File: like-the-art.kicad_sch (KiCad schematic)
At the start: 4 parts

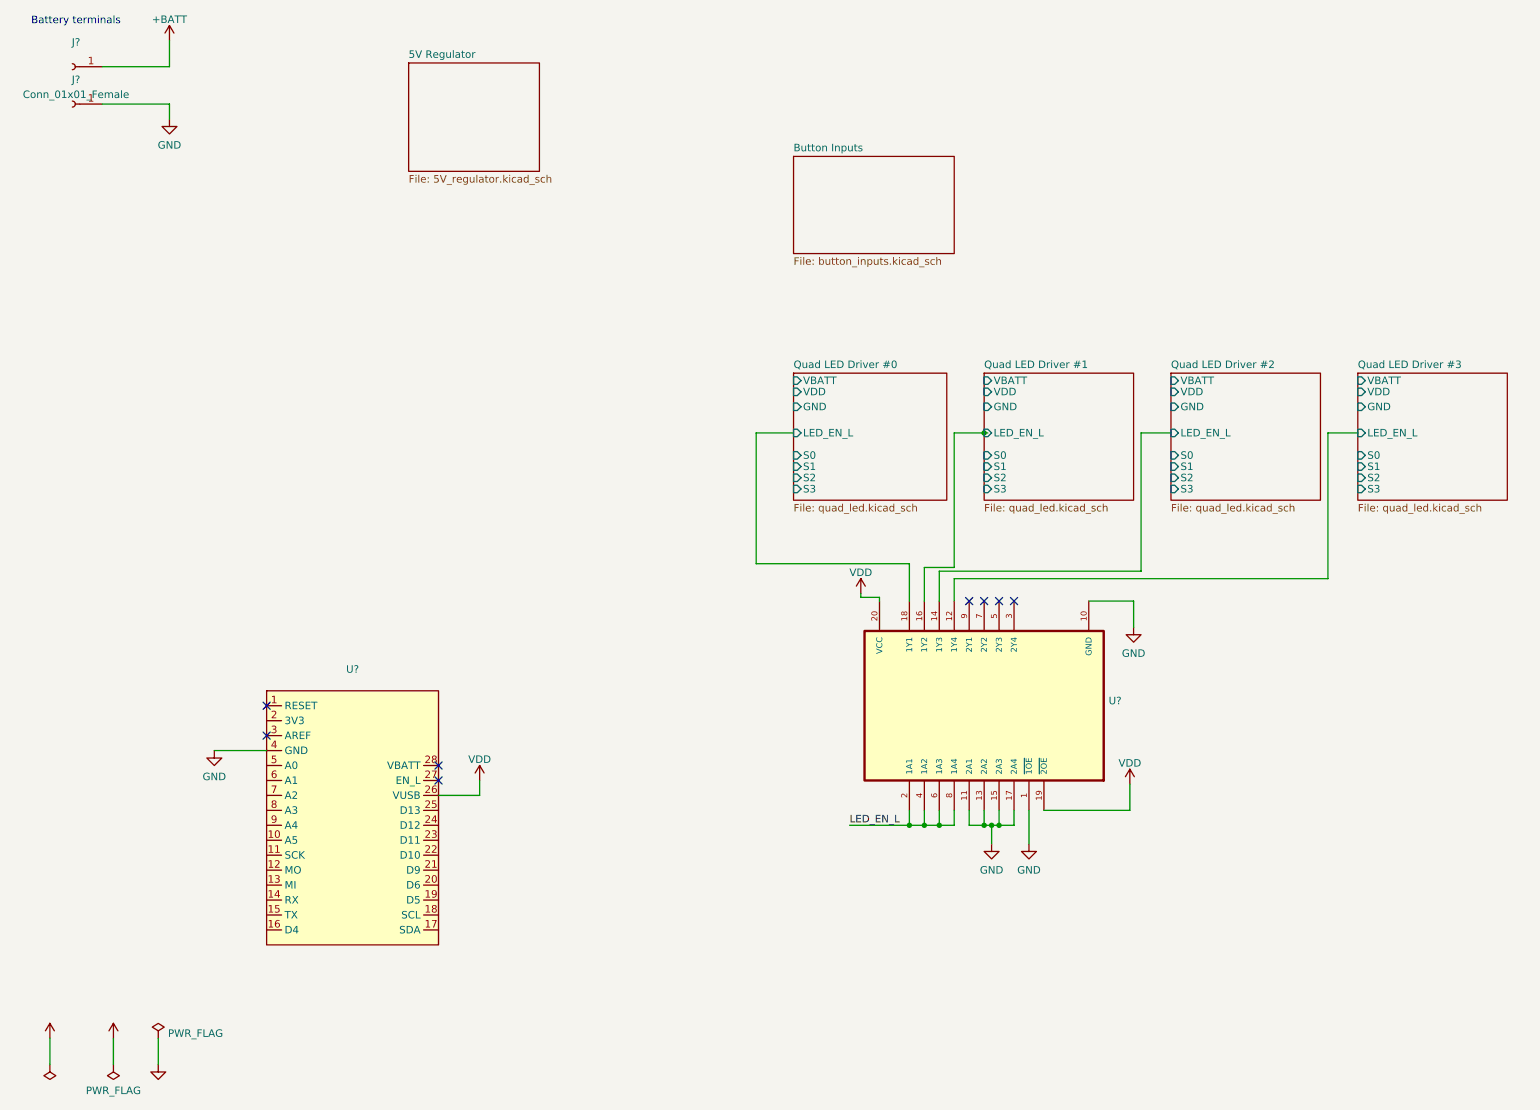
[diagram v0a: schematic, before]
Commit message: Add schematic for button inputs and I2C signal busses.
* Define 9x button inputs
* Define I2C parallel bus expanders used for FET output signals
  and button inputs
* Add (empty) schematic for 5V switching regulator.
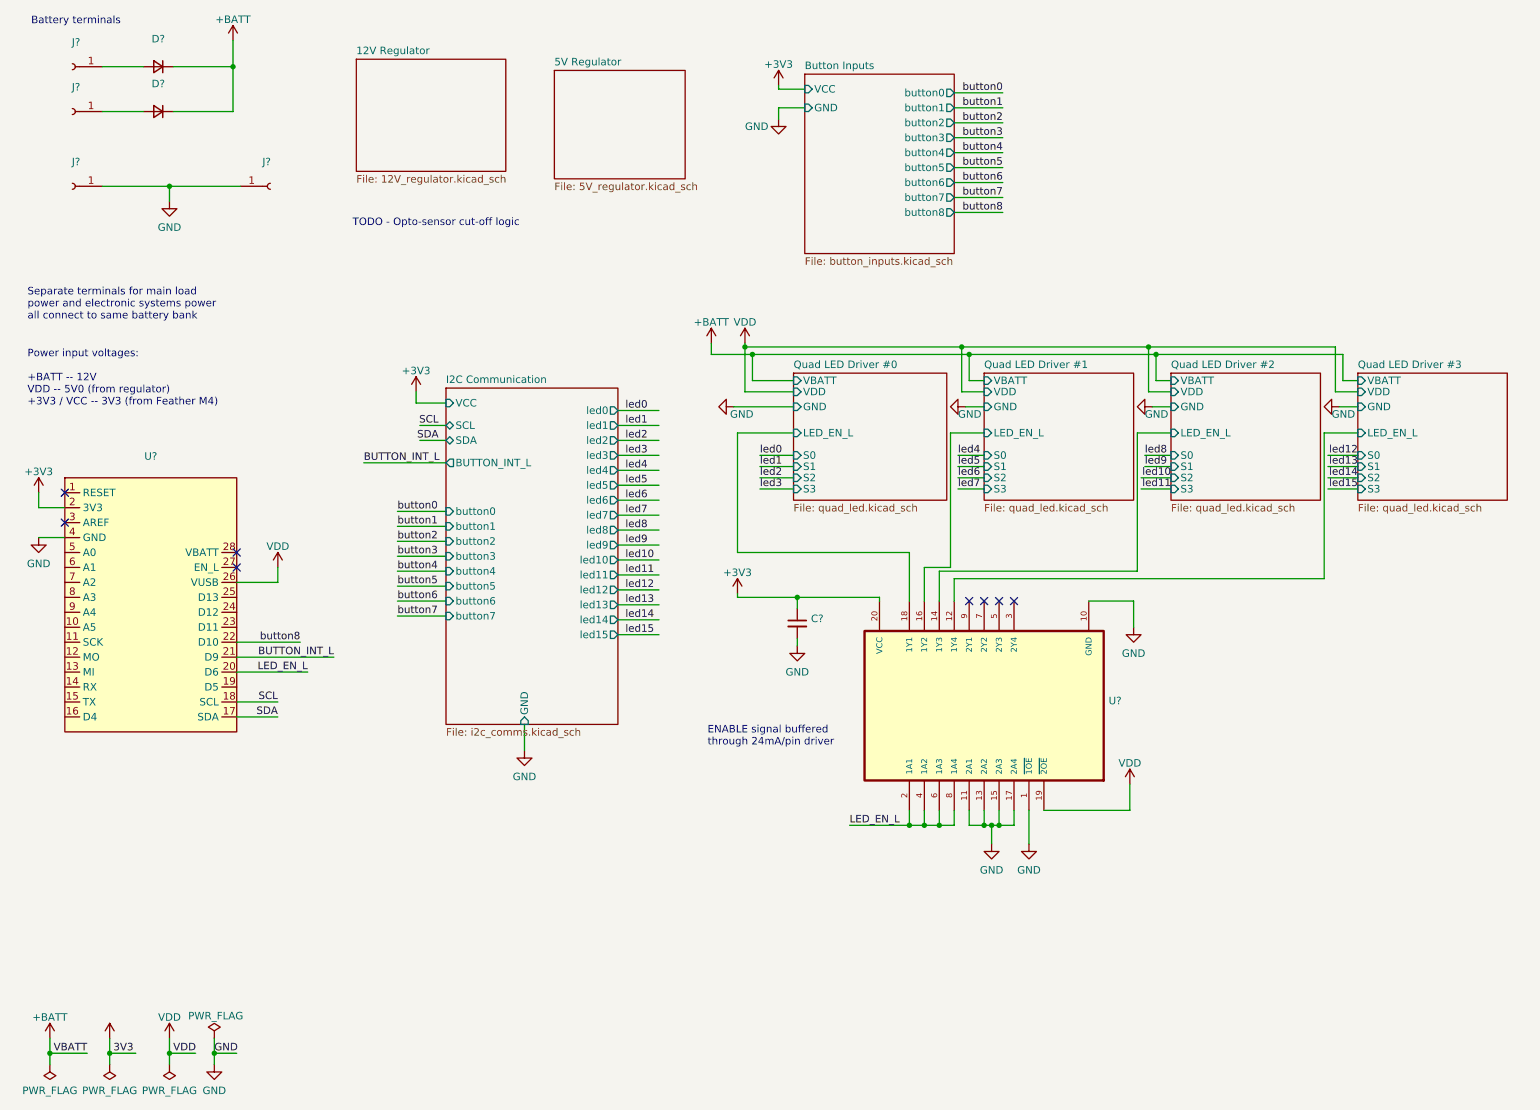
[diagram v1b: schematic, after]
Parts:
- added C?: (no value), symbol Device:C_Small
- added D? (x2): (no value), symbol Device:D_Small
- added J? (x2): (no value), symbol Connector:Conn_01x01_Female
- J?: value Conn_01x01_Female -> (none)
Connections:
- net +BATT: now also D?.1 (K), D?.1 (K); no longer J?.1 (Pin_1)
- net GND: now also C?.2, J?.1 (Pin_1)
- net LED_EN_L: now also U?.20 (D6)
- net VDD: no longer U?.20 (VCC)
- net SDA: now reaches U?.17 (SDA)
- net SCL: now reaches U?.18 (SCL)
- net +3V3: now reaches U?.2 (3V3)
- net +3V3: now also U?.20 (VCC), C?.1
- net BUTTON_INT_L: now reaches U?.21 (D9)
- net button8: now reaches U?.22 (D10)
- new net: D?.2 (A), J?.1 (Pin_1) (x2)
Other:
- added sheet 12V Regulator (12V_regulator.kicad_sch)
- added sheet I2C Communication (i2c_comms.kicad_sch)
- sheet Button Inputs ports: added GND, VCC, button0, button1, button2, button3, button4, button5, button6, button7, button8; removed none
- note added: "ENABLE signal buffered through 24mA/pin driver"
- note added: "Power input voltages: +BATT -- 12V VDD -- 5V0 (from regulator) +3V3 / VCC -- 3V3 (from Feather M4)"
- note added: "Separate terminals for main load power and electronic systems power all connect to same battery bank"
- note added: "TODO - Opto-sensor cut-off logic"
- moved on the sheet: J?, U?

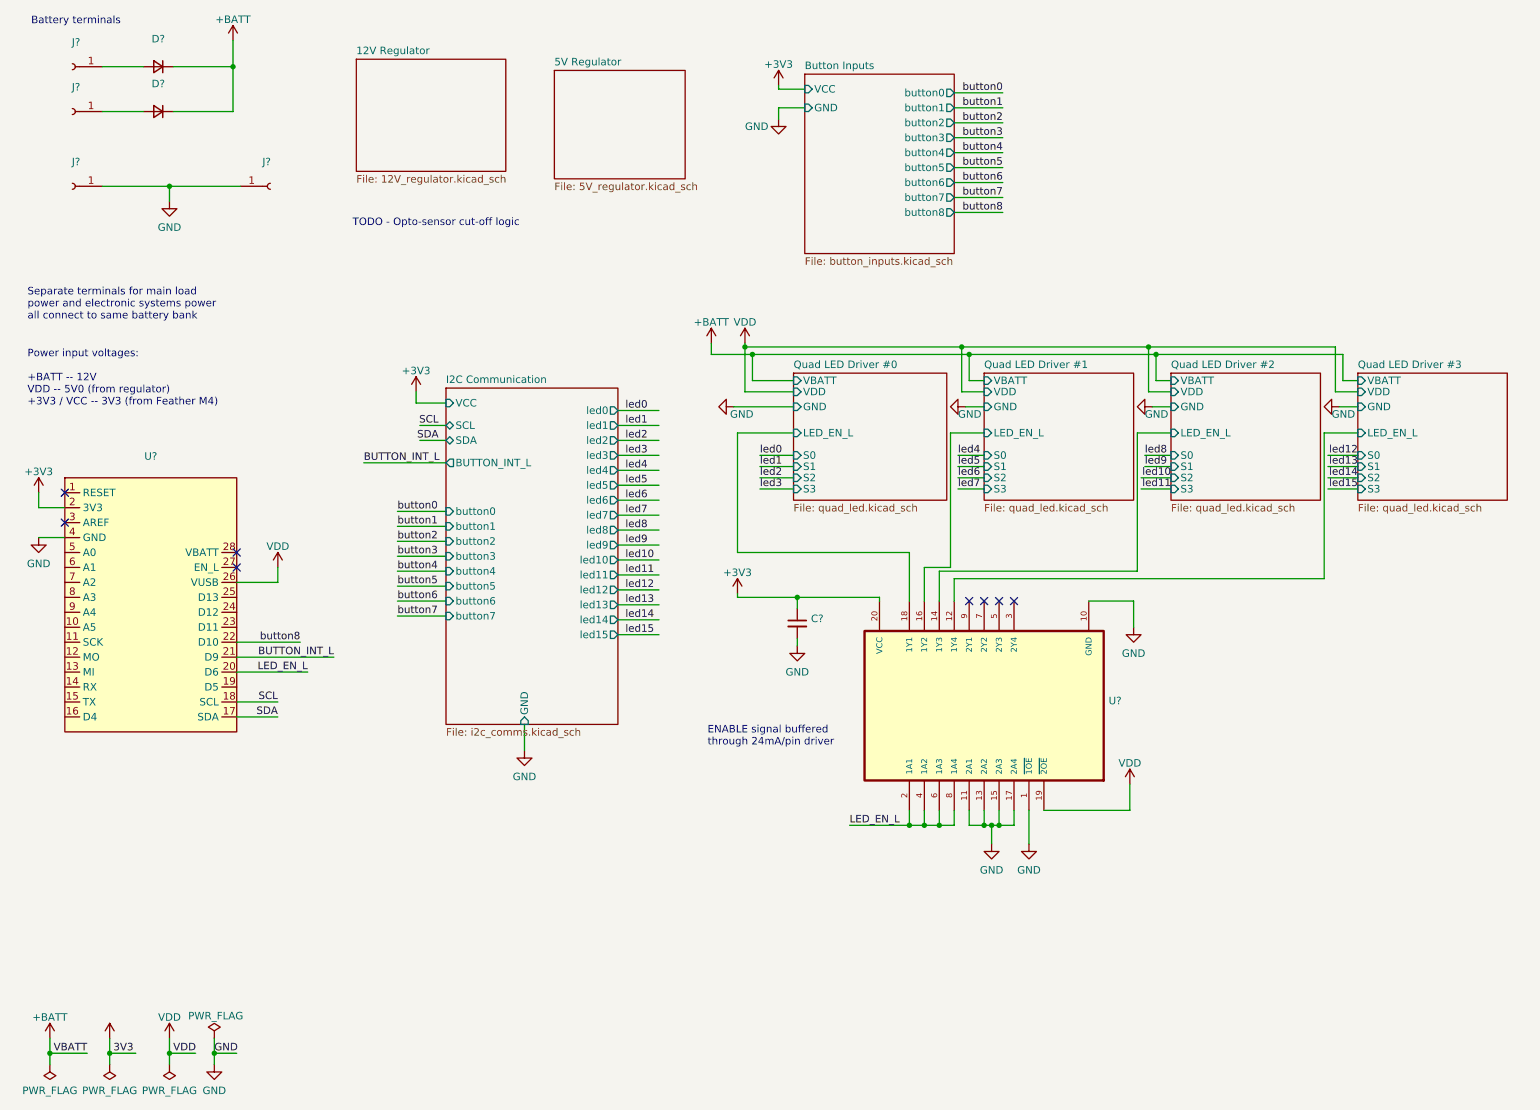
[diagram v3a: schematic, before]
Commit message: Sketch out ISL8117-driven 12V regulator.
Another candidate entry for on-board 12V regulation is to
build our own based on the reference schematic from the ISL8117
DC buck regulator controller datasheet.

Implemented (most of) this reference schematic here.
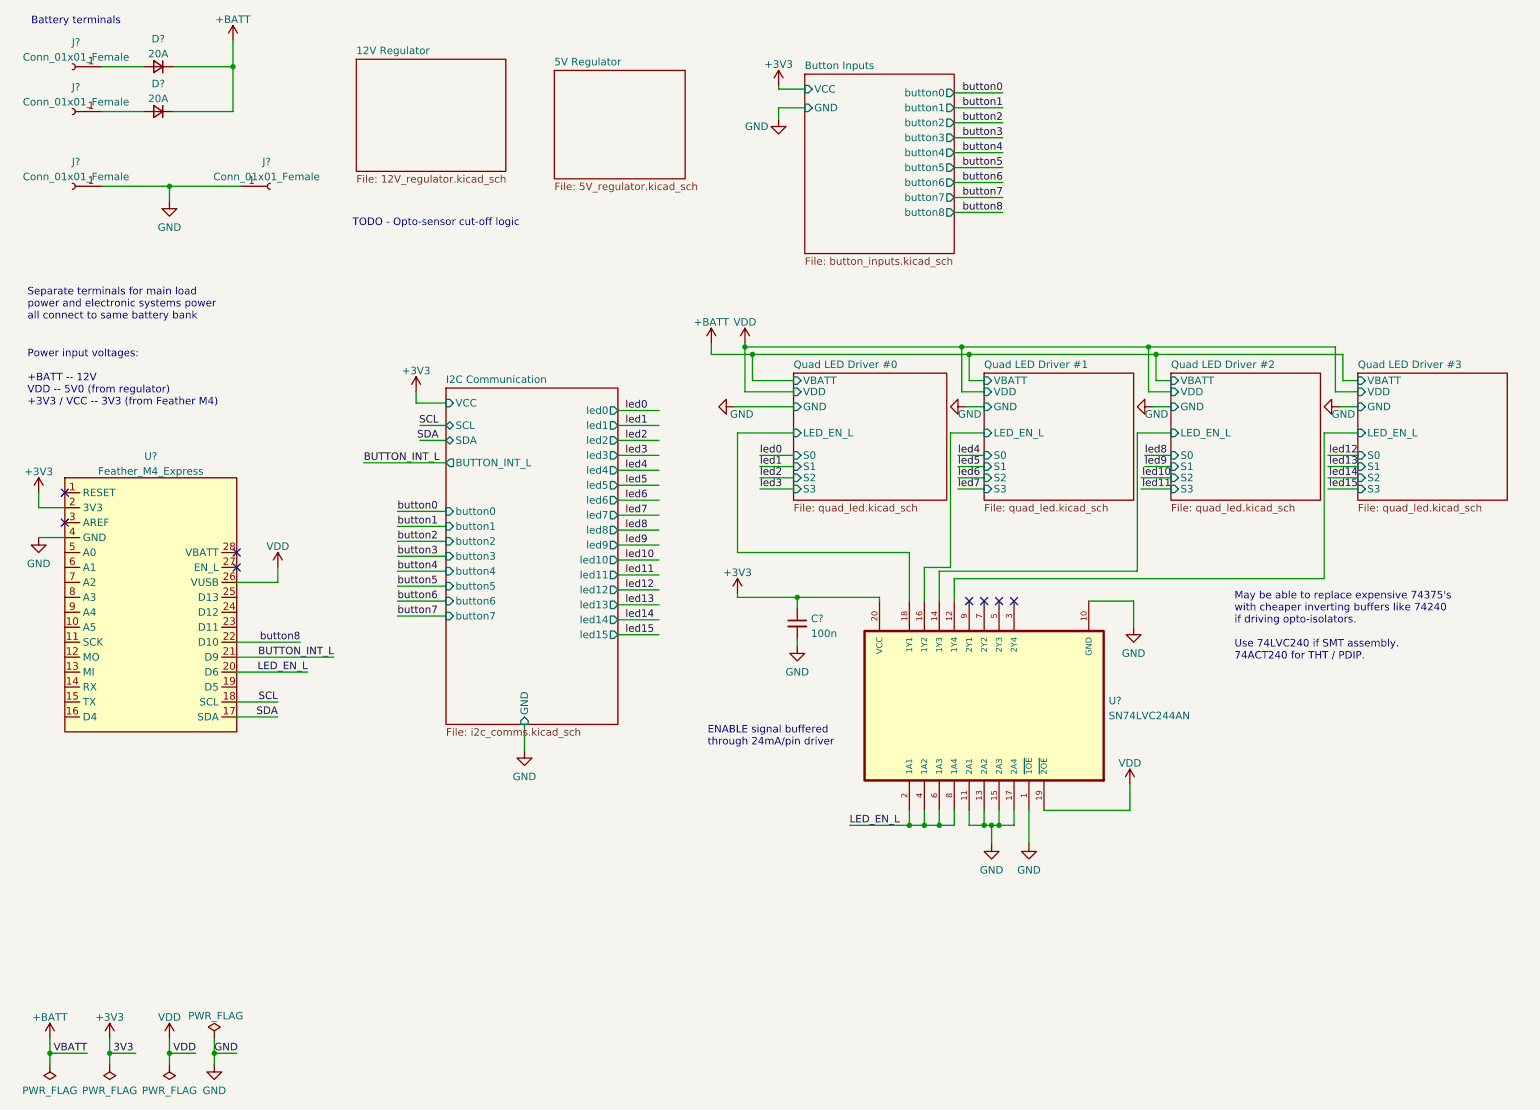
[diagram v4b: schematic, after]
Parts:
- C?: value (none) -> 100n
- D? (x2): value (none) -> 20A
- J? (x4): value (none) -> Conn_01x01_Female
- U?: value (none) -> SN74LVC244AN; footprint (none) -> Aaron_TI_Parts:TI_N_R-PDIP-T20
- U?: value (none) -> Feather_M4_Express; footprint (none) -> aaron-imported-parts:Arduino_Feather_M4_Express_PinHeaders
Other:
- note added: "May be able to replace expensive 74375's with cheaper inverting buffers like 74240 if driving opto-isolators. Use 74LVC240 if SMT assembly. 74ACT240 for THT / PDIP."
